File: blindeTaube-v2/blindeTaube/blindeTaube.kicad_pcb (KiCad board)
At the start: 2 copper layers, 26.2 x 104.5 mm, 122 parts, among them J1 AudioJack2_SwitchT, J13 Conn_02x05_Odd_Even, J2 AudioJack2_SwitchT, J3 AudioJack2_SwitchT, J4 Conn_01x01_Male, J5 AudioJack2_SwitchT, J6 AudioJack2_SwitchT, J7 AudioJack2_SwitchT, J8 Conn_01x01_Male, J9 Conn_01x01_Male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

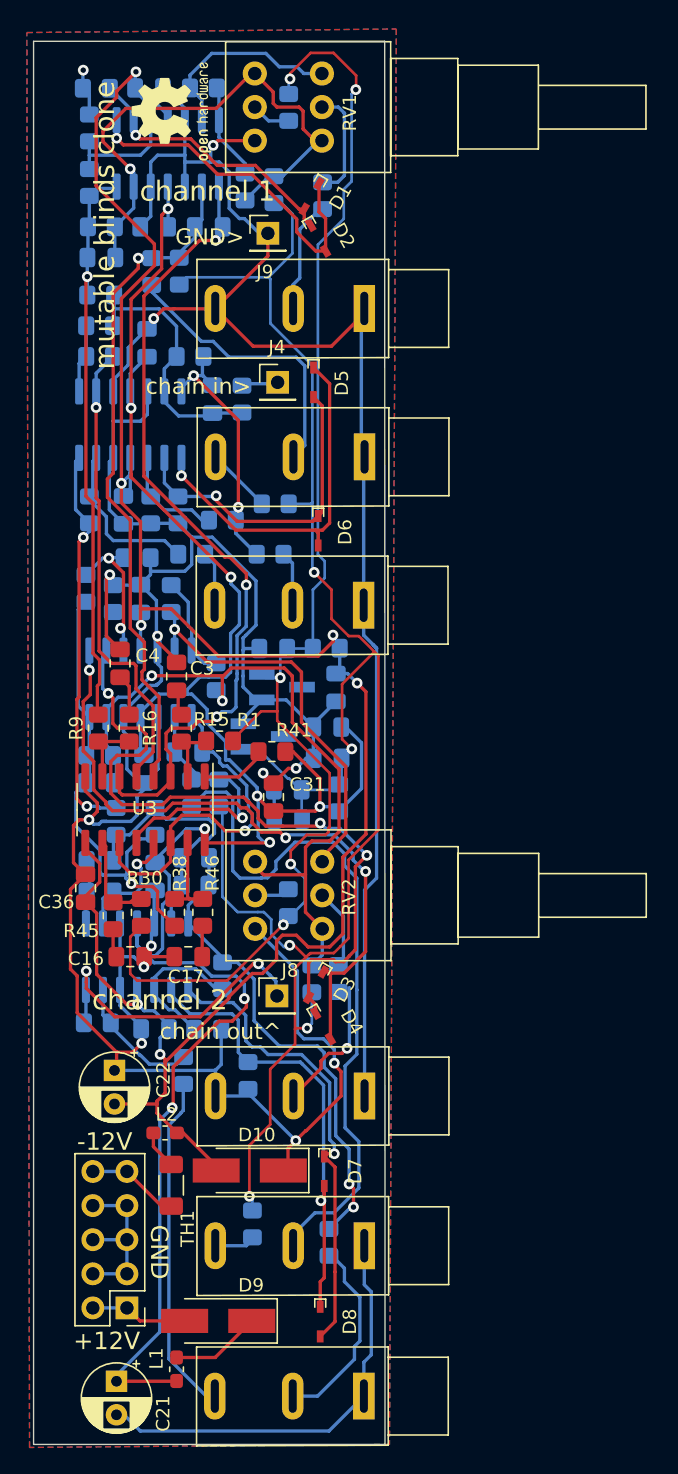
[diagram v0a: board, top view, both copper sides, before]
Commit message: move potentiometers a little bit to the edge of the board
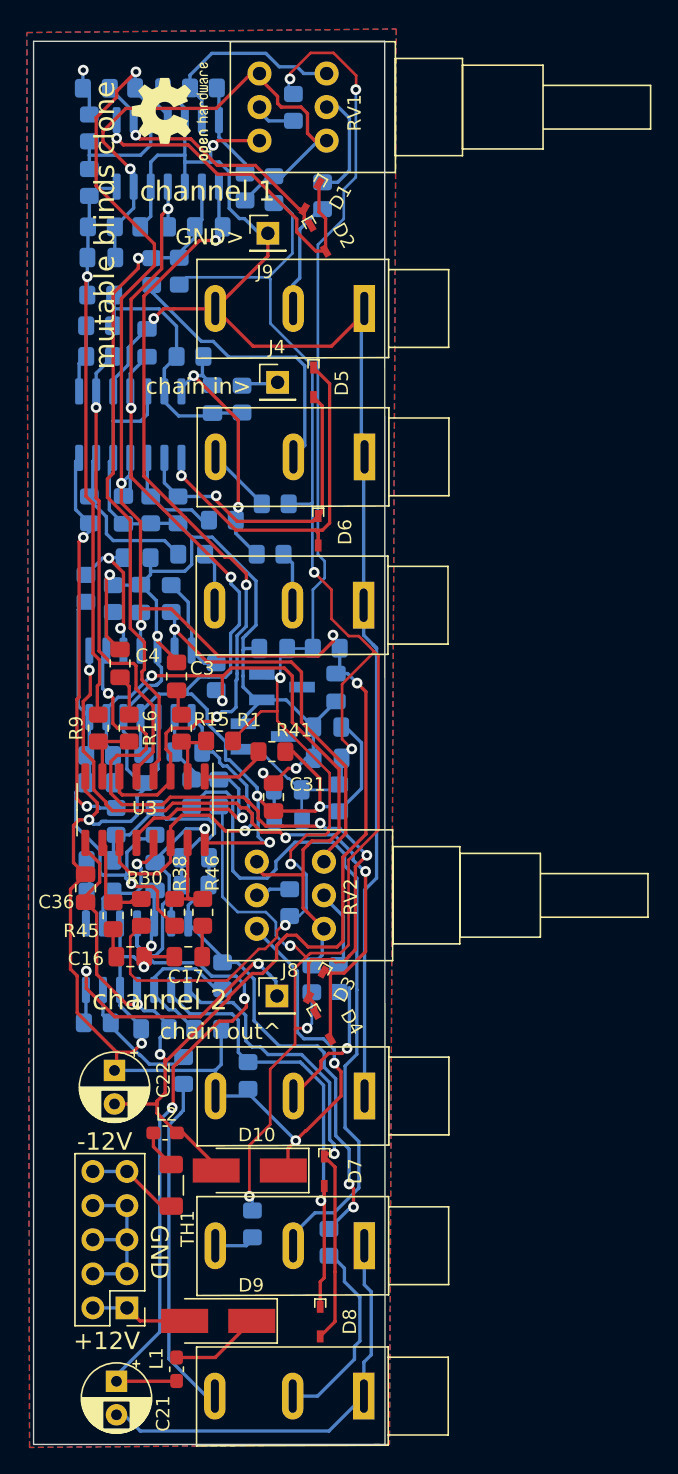
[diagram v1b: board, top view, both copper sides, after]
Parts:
- moved RV1 0.35 mm to (75.1, 48.7)
- moved R13 0.35 mm to (72.6, 46.2)
- moved RV2 0.12 mm to (74.9, 107.4)
- moved R43 0.10 mm to (72.3, 105.5)
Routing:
- net VEE: track 153.0 -> 154.1 mm
- net AREF_-10: track 103.4 -> 104.4 mm
